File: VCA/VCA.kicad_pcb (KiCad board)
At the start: 2 copper layers, 40 x 200 mm, 57 parts, among them J1 EuroPower, J2 CV1, J3 IN1, J4 OUT1, J5 CV2, J6 IN2, J7 OUT2, U1 LM13700, U2 TL082, U3 TL082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

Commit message: updated footprints on VCA
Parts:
- J2, J3, J4, J5, J6, J7: footprint telec:JackHole -> telec:Jack_Hole_Square
- RV1, RV2, RV4, RV5: footprint Potentiometer_THT:Potentiometer_Piher_T-16L_Single_Vertical_Hole -> telec:Potentiometer_Single_Vertical_Hole
- moved RV4 13.3 mm to (41.7, 139.7), turned to 0 degrees
- moved RV5 13.1 mm to (22.1, 139.7), turned to 0 degrees
- moved RV1 12.9 mm to (42.0, 41.4), turned to 0 degrees
- moved RV2 12.8 mm to (22.6, 41.3), turned to 0 degrees
- moved R18 3.41 mm to (32.4, 136.6), turned to 90 degrees
- moved C2 1.50 mm to (39.5, 130.5)
- moved R8 0.31 mm to (43.2, 57.4)
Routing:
- net +12V: track 244.5 -> 250.5 mm
- net /IN1: track 32.2 -> 27.6 mm
- net /IN2: track 32.2 -> 27.6 mm
- net -12V: track 175.6 -> 177.9 mm
- net /CV2: track 25.5 -> 27.3 mm
- net GND: track 3.61 -> 2.37 mm
- net Net-(R18-Pad2): track 2.52 -> 3.63 mm
- net Net-(R19-Pad2): track 25.1 -> 26.2 mm
- net Net-(R12-Pad1): track 16.6 -> 15.7 mm
- net Net-(J4-PadT): track 4.30 -> 5.16 mm
- net Net-(R1-Pad1): track 15.7 -> 15.1 mm
- net /CV1: track 25.6 -> 26.1 mm
- net (no net): vias 0 -> 1

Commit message: VCA ready for prod
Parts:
- R10: value 150k -> 120k
- R11: value 27k -> 220k
- R7: value 10k -> 12k
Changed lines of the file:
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@@
   )
   (setup
-    (last_trace_width 1.016)
+    (last_trace_width 0.1524)
     (user_trace_width 0.1524)
     (user_trace_width 0.254)
@@
       (effects (font (size 1 1) (thickness 0.15)) (justify mirror))
     )
-    (fp_text value 10k (at 0 1.82) (layer B.SilkS)
+    (fp_text value 12k (at 0 1.82) (layer B.SilkS)
       (effects (font (size 1 1) (thickness 0.15)) (justify mirror))
     )
@@
       (effects (font (size 1 1) (thickness 0.15)) (justify mirror))
     )
-    (fp_text value 27k (at 0.1125 1.4) (layer B.SilkS)
+    (fp_text value 220k (at 0.1125 1.4) (layer B.SilkS)
       (effects (font (size 1 1) (thickness 0.15)) (justify mirror))
     )
@@
       (effects (font (size 1 1) (thickness 0.15)) (justify mirror))
     )
-    (fp_text value 150k (at 1.4875 1.6) (layer B.SilkS)
+    (fp_text value 120k (at 1.4875 1.6) (layer B.SilkS)
       (effects (font (size 1 1) (thickness 0.15)) (justify mirror))
     )
@@
     (arrow2b (pts (xy 12 6) (xy 13.126504 5.413579)))
   )
+  (via (at 46.6 60.4) (size 0.8) (drill 0.4) (layers F.Cu B.Cu) (net 0))
   (via (at 14.5 107.5) (size 0.8) (drill 0.4) (layers F.Cu B.Cu) (net 1))
   (via (at 33.2 107.7) (size 0.8) (drill 0.4) (layers F.Cu B.Cu) (net 1))
@@
   (segment (start 29.3 103.7) (end 32.4 100.6) (width 0.508) (layer F.Cu) (net 1))
   (segment (start 32.4 100.6) (end 32.4 97.5) (width 0.508) (layer F.Cu) (net 1))
+  (segment (start 48.169999 52.230001) (end 47 53.4) (width 1.016) (layer F.Cu) (net 1))
+  (segment (start 27.9 27.3) (end 27.9 24.304) (width 1.016) (layer F.Cu) (net 1))
+  (segment (start 28.968001 23.235999) (end 38.791521 23.235999) (width 1.016) (layer F.Cu) (net 1))
+  (segment (start 27.9 24.304) (end 28.968001 23.235999) (width 1.016) (layer F.Cu) (net 1))
+  (segment (start 38.791521 23.235999) (end 48.169999 32.614477) (width 1.016) (layer F.Cu) (net 1))
+  (segment (start 38.125 62.925) (end 39.395 62.925) (width 1.016) (layer F.Cu) (net 1))
+  (segment (start 39.5 55.2) (end 36.5 58.2) (width 1.016) (layer F.Cu) (net 1))
+  (segment (start 48.169999 32.614477) (end 48.169999 44.130001) (width 1.016) (layer F.Cu) (net 1))
+  (segment (start 36.5 58.2) (end 36.5 61.3) (width 1.016) (layer F.Cu) (net 1))
+  (segment (start 48.169999 44.130001) (end 48.169999 46.630001) (width 1.016) (layer F.Cu) (net 1))
+  (segment (start 36.5 61.3) (end 38.125 62.925) (width 1.016) (layer F.Cu) (net 1))
+  (segment (start 39.5 52.4) (end 39.5 55.2) (width 1.016) (layer F.Cu) (net 1))
+  (segment (start 48.169999 44.130001) (end 48.169999 52.230001) (width 1.016) (layer F.Cu) (net 1))
+  (segment (start 41.2 50.7) (end 39.5 52.4) (width 1.016) (layer F.Cu) (net 1))
+  (segment (start 48.169999 46.630001) (end 44.1 50.7) (width 1.016) (layer F.Cu) (net 1))
+  (segment (start 44.1 50.7) (end 41.2 50.7) (width 1.016) (layer F.Cu) (net 1))
+  (segment (start 44.299291 149.299291) (end 46.7 151.7) (width 1.016) (layer F.Cu) (net 1))
+  (segment (start 37.300709 149.299291) (end 44.299291 149.299291) (width 1.016) (layer F.Cu) (net 1))
+  (segment (start 37.300709 149.299291) (end 37.9 149.9) (width 1.016) (layer F.Cu) (net 1))
+  (segment (start 34.1 146.091006) (end 37.300709 149.299291) (width 1.016) (layer F.Cu) (net 1))
+  (via (at 32.4 138.0875) (size 0.8) (drill 0.4) (layers F.Cu B.Cu) (net 1))
+  (segment (start 36.575 128.45) (end 36.575 133.9125) (width 1.016) (layer B.Cu) (net 1))
+  (segment (start 36.575 133.9125) (end 32.4 138.0875) (width 1.016) (layer B.Cu) (net 1))
+  (segment (start 32.4 144.391006) (end 34.1 146.091006) (width 1.016) (layer F.Cu) (net 1))
+  (segment (start 32.4 138.0875) (end 32.4 144.391006) (width 1.016) (layer F.Cu) (net 1))
   (via (at 40 132.6) (size 0.8) (drill 0.4) (layers F.Cu B.Cu) (net 2))
   (via (at 40 126.5) (size 0.8) (drill 0.4) (layers F.Cu B.Cu) (net 2))
@@
   (via (at 50.6 69.2) (size 0.8) (drill 0.4) (layers F.Cu B.Cu) (net 2))
   (via (at 50.9 60.1) (size 0.8) (drill 0.4) (layers F.Cu B.Cu) (net 2))
-  (via (at 46.6 60.4) (size 0.8) (drill 0.4) (layers F.Cu B.Cu) (net 0))
-  (segment (start 48.169999 52.230001) (end 47 53.4) (width 1.016) (layer F.Cu) (net 1))
-  (segment (start 27.9 27.3) (end 27.9 24.304) (width 1.016) (layer F.Cu) (net 1))
-  (segment (start 28.968001 23.235999) (end 38.791521 23.235999) (width 1.016) (layer F.Cu) (net 1))
-  (segment (start 27.9 24.304) (end 28.968001 23.235999) (width 1.016) (layer F.Cu) (net 1))
-  (segment (start 38.791521 23.235999) (end 48.169999 32.614477) (width 1.016) (layer F.Cu) (net 1))
-  (segment (start 38.125 62.925) (end 39.395 62.925) (width 1.016) (layer F.Cu) (net 1))
-  (segment (start 39.5 55.2) (end 36.5 58.2) (width 1.016) (layer F.Cu) (net 1))
-  (segment (start 48.169999 32.614477) (end 48.169999 44.130001) (width 1.016) (layer F.Cu) (net 1))
-  (segment (start 36.5 58.2) (end 36.5 61.3) (width 1.016) (layer F.Cu) (net 1))
-  (segment (start 48.169999 44.130001) (end 48.169999 46.630001) (width 1.016) (layer F.Cu) (net 1))
-  (segment (start 36.5 61.3) (end 38.125 62.925) (width 1.016) (layer F.Cu) (net 1))
-  (segment (start 39.5 52.4) (end 39.5 55.2) (width 1.016) (layer F.Cu) (net 1))
-  (segment (start 48.169999 44.130001) (end 48.169999 52.230001) (width 1.016) (layer F.Cu) (net 1))
-  (segment (start 41.2 50.7) (end 39.5 52.4) (width 1.016) (layer F.Cu) (net 1))
-  (segment (start 48.169999 46.630001) (end 44.1 50.7) (width 1.016) (layer F.Cu) (net 1))
-  (segment (start 44.1 50.7) (end 41.2 50.7) (width 1.016) (layer F.Cu) (net 1))
-  (segment (start 44.299291 149.299291) (end 46.7 151.7) (width 1.016) (layer F.Cu) (net 1))
-  (segment (start 37.300709 149.299291) (end 44.299291 149.299291) (width 1.016) (layer F.Cu) (net 1))
-  (segment (start 37.300709 149.299291) (end 37.9 149.9) (width 1.016) (layer F.Cu) (net 1))
-  (segment (start 34.1 146.091006) (end 37.300709 149.299291) (width 1.016) (layer F.Cu) (net 1))
-  (via (at 32.4 138.0875) (size 0.8) (drill 0.4) (layers F.Cu B.Cu) (net 1))
-  (segment (start 36.575 128.45) (end 36.575 133.9125) (width 1.016) (layer B.Cu) (net 1))
-  (segment (start 36.575 133.9125) (end 32.4 138.0875) (width 1.016) (layer B.Cu) (net 1))
-  (segment (start 32.4 144.391006) (end 34.1 146.091006) (width 1.016) (layer F.Cu) (net 1))
-  (segment (start 32.4 138.0875) (end 32.4 144.391006) (width 1.016) (layer F.Cu) (net 1))
   (via (at 48.6 89.2) (size 0.8) (drill 0.4) (layers F.Cu B.Cu) (net 2))
   (via (at 48.6 97.7) (size 0.8) (drill 0.4) (layers F.Cu B.Cu) (net 2))

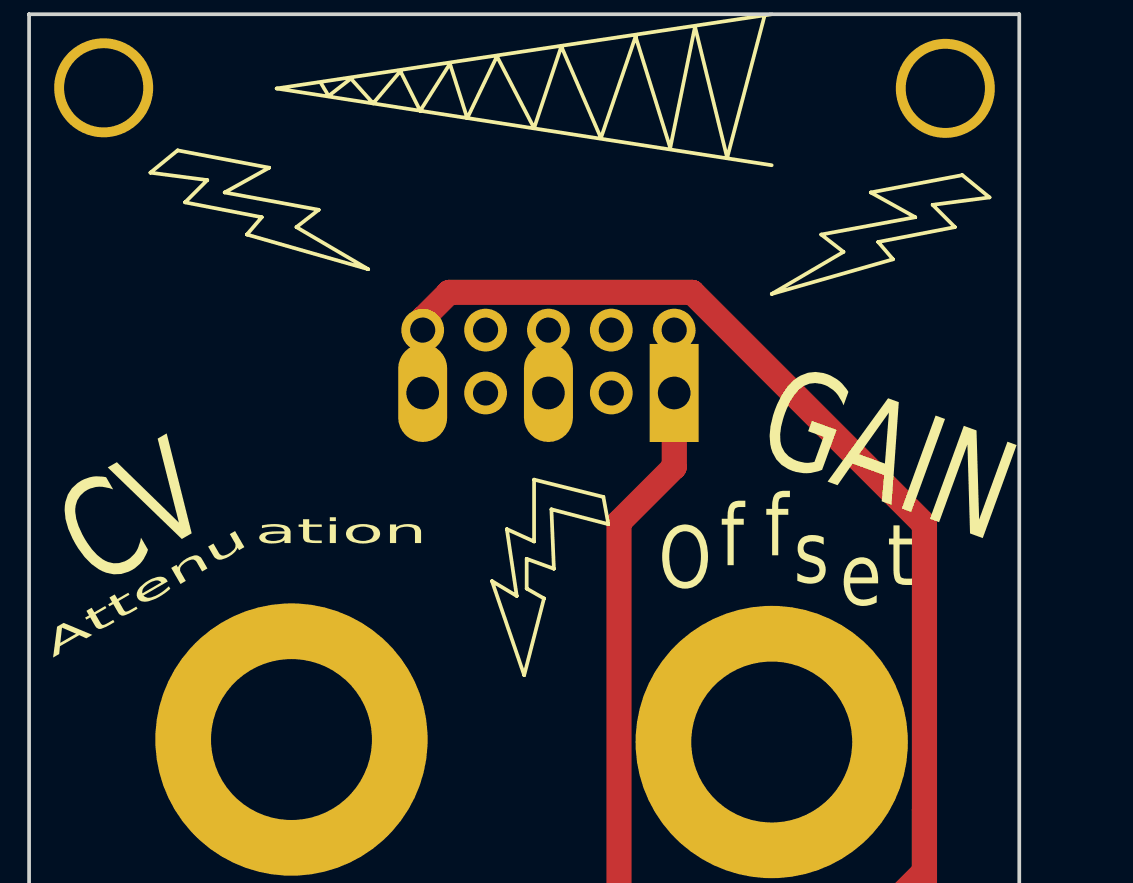
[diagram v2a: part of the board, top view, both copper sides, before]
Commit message: More clearance
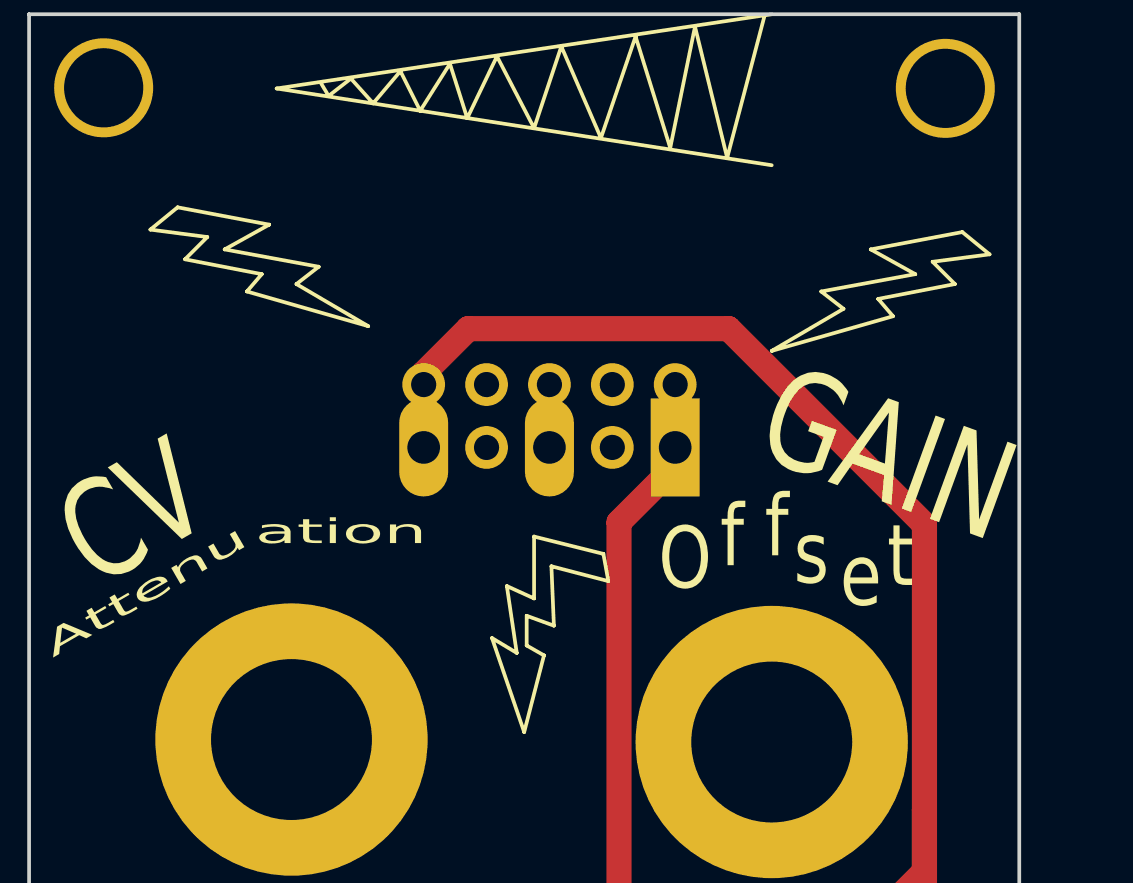
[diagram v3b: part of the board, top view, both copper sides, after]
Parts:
- moved J1 2.20 mm to (38.1, 29.5)
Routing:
- net -12V: track 177.9 -> 175.4 mm
- net +12V: track 250.5 -> 252.7 mm
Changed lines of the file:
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@@
   (general
     (thickness 1.6)
-    (drawings 154)
+    (drawings 157)
     (tracks 356)
     (zones 0)
@@
   )
   (setup
-    (last_trace_width 0.1524)
+    (last_trace_width 1.016)
     (user_trace_width 0.1524)
     (user_trace_width 0.254)
@@
   )
   (module telec:EuroPower (layer B.Cu)
-    (at 38.06 27.3 90)
+    (at 38.1 29.5 90)
     (fp_text reference J1 (at 1.397 6.35 270) (layer B.SilkS)
       (effects (font (size 1 1) (thickness 0.15)) (justify mirror))
@@
       (rotate (xyz 0 0 0))
     )
+  )
+  (gr_line (start 52 23) (end 11.9 23) (layer F.Fab) (width 0.15))
+  (dimension 11 (width 0.15) (layer F.Fab)
+    (gr_text "11,000 mm" (at 55.7 17.5 270) (layer F.Fab)
+      (effects (font (size 1 1) (thickness 0.15)))
+    )
+    (feature1 (pts (xy 52 23) (xy 54.986421 23)))
+    (feature2 (pts (xy 52 12) (xy 54.986421 12)))
+    (crossbar (pts (xy 54.4 12) (xy 54.4 23)))
+    (arrow1a (pts (xy 54.4 23) (xy 53.813579 21.873496)))
+    (arrow1b (pts (xy 54.4 23) (xy 54.986421 21.873496)))
+    (arrow2a (pts (xy 54.4 12) (xy 53.813579 13.126504)))
+    (arrow2b (pts (xy 54.4 12) (xy 54.986421 13.126504)))
+  )
+  (dimension 12.7 (width 0.15) (layer F.Fab)
+    (gr_text "12,700 mm" (at 55.1 205.65 90) (layer F.Fab)
+      (effects (font (size 1 1) (thickness 0.15)))
+    )
+    (feature1 (pts (xy 52 199.3) (xy 54.386421 199.3)))
+    (feature2 (pts (xy 52 212) (xy 54.386421 212)))
+    (crossbar (pts (xy 53.8 212) (xy 53.8 199.3)))
+    (arrow1a (pts (xy 53.8 199.3) (xy 54.386421 200.426504)))
+    (arrow1b (pts (xy 53.8 199.3) (xy 53.213579 200.426504)))
+    (arrow2a (pts (xy 53.8 212) (xy 54.386421 210.873496)))
+    (arrow2b (pts (xy 53.8 212) (xy 53.213579 210.873496)))
   )
   (gr_line (start 12.3 202.8) (end 32.1 202.8) (layer F.SilkS) (width 0.5))
@@
     (effects (font (size 4 3) (thickness 0.4)))
   )
-  (gr_line (start 46 19.2) (end 47.8 20.2) (layer F.SilkS) (width 0.15))
-  (gr_line (start 47.8 20.2) (end 44 20.9) (layer F.SilkS) (width 0.15))
-  (gr_line (start 46.3 21.2) (end 49.4 20.6) (layer F.SilkS) (width 0.15))
-  (gr_line (start 44.9 21.6) (end 42 23.3) (layer F.SilkS) (width 0.15))
-  (gr_line (start 44 20.9) (end 44.9 21.6) (layer F.SilkS) (width 0.15))
-  (gr_line (start 49.4 20.6) (end 48.5 19.7) (layer F.SilkS) (width 0.15))
-  (gr_line (start 48.5 19.7) (end 50.8 19.4) (layer F.SilkS) (width 0.15))
-  (gr_line (start 46.9 21.9) (end 46.3 21.2) (layer F.SilkS) (width 0.15))
-  (gr_line (start 50.8 19.4) (end 49.7 18.5) (layer F.SilkS) (width 0.15))
-  (gr_line (start 42 23.3) (end 46.9 21.9) (layer F.SilkS) (width 0.15))
-  (gr_line (start 49.7 18.5) (end 46 19.2) (layer F.SilkS) (width 0.15))
-  (gr_line (start 35.4 32.6) (end 35.2 31.5) (layer F.SilkS) (width 0.15))
-  (gr_line (start 33.1 32) (end 35.4 32.6) (layer F.SilkS) (width 0.15))
-  (gr_line (start 33.2 34.4) (end 33.1 32) (layer F.SilkS) (width 0.15))
-  (gr_line (start 32.1 34) (end 33.2 34.4) (layer F.SilkS) (width 0.15))
-  (gr_line (start 32.1 35.2) (end 32.1 34) (layer F.SilkS) (width 0.15))
-  (gr_line (start 32.8 35.6) (end 32.1 35.2) (layer F.SilkS) (width 0.15))
-  (gr_line (start 32 38.7) (end 32.8 35.6) (layer F.SilkS) (width 0.15))
-  (gr_line (start 30.7 34.9) (end 32 38.7) (layer F.SilkS) (width 0.15))
-  (gr_line (start 31.7 35.5) (end 30.7 34.9) (layer F.SilkS) (width 0.15))
-  (gr_line (start 31.3 32.8) (end 31.7 35.5) (layer F.SilkS) (width 0.15))
-  (gr_line (start 32.4 33.3) (end 31.3 32.8) (layer F.SilkS) (width 0.15))
-  (gr_line (start 32.4 30.8) (end 32.4 33.3) (layer F.SilkS) (width 0.15))
-  (gr_line (start 35.2 31.5) (end 32.4 30.8) (layer F.SilkS) (width 0.15))
-  (gr_line (start 19.2 18.7) (end 16.9 18.4) (layer F.SilkS) (width 0.15))
-  (gr_line (start 18.3 19.6) (end 19.2 18.7) (layer F.SilkS) (width 0.15))
-  (gr_line (start 21.4 20.2) (end 18.3 19.6) (layer F.SilkS) (width 0.15))
-  (gr_line (start 20.8 20.9) (end 21.4 20.2) (layer F.SilkS) (width 0.15))
-  (gr_line (start 25.7 22.3) (end 20.8 20.9) (layer F.SilkS) (width 0.15))
-  (gr_line (start 22.8 20.6) (end 25.7 22.3) (layer F.SilkS) (width 0.15))
-  (gr_line (start 23.7 19.9) (end 22.8 20.6) (layer F.SilkS) (width 0.15))
-  (gr_line (start 19.9 19.2) (end 23.7 19.9) (layer F.SilkS) (width 0.15))
-  (gr_line (start 21.7 18.2) (end 19.9 19.2) (layer F.SilkS) (width 0.15))
-  (gr_line (start 18 17.5) (end 21.7 18.2) (layer F.SilkS) (width 0.15))
-  (gr_line (start 16.9 18.4) (end 18 17.5) (layer F.SilkS) (width 0.15))
+  (gr_line (start 46 21.5) (end 47.8 22.5) (layer F.SilkS) (width 0.15))
+  (gr_line (start 47.8 22.5) (end 44 23.2) (layer F.SilkS) (width 0.15))
+  (gr_line (start 46.3 23.5) (end 49.4 22.9) (layer F.SilkS) (width 0.15))
+  (gr_line (start 44.9 23.9) (end 42 25.6) (layer F.SilkS) (width 0.15))
+  (gr_line (start 44 23.2) (end 44.9 23.9) (layer F.SilkS) (width 0.15))
+  (gr_line (start 49.4 22.9) (end 48.5 22) (layer F.SilkS) (width 0.15))
+  (gr_line (start 48.5 22) (end 50.8 21.7) (layer F.SilkS) (width 0.15))
+  (gr_line (start 46.9 24.2) (end 46.3 23.5) (layer F.SilkS) (width 0.15))
+  (gr_line (start 50.8 21.7) (end 49.7 20.8) (layer F.SilkS) (width 0.15))
+  (gr_line (start 42 25.6) (end 46.9 24.2) (layer F.SilkS) (width 0.15))
+  (gr_line (start 49.7 20.8) (end 46 21.5) (layer F.SilkS) (width 0.15))
+  (gr_line (start 35.4 34.9) (end 35.2 33.8) (layer F.SilkS) (width 0.15))
+  (gr_line (start 33.1 34.3) (end 35.4 34.9) (layer F.SilkS) (width 0.15))
+  (gr_line (start 33.2 36.7) (end 33.1 34.3) (layer F.SilkS) (width 0.15))
+  (gr_line (start 32.1 36.3) (end 33.2 36.7) (layer F.SilkS) (width 0.15))
+  (gr_line (start 32.1 37.5) (end 32.1 36.3) (layer F.SilkS) (width 0.15))
+  (gr_line (start 32.8 37.9) (end 32.1 37.5) (layer F.SilkS) (width 0.15))
+  (gr_line (start 32 41) (end 32.8 37.9) (layer F.SilkS) (width 0.15))
+  (gr_line (start 30.7 37.2) (end 32 41) (layer F.SilkS) (width 0.15))
+  (gr_line (start 31.7 37.8) (end 30.7 37.2) (layer F.SilkS) (width 0.15))
+  (gr_line (start 31.3 35.1) (end 31.7 37.8) (layer F.SilkS) (width 0.15))
+  (gr_line (start 32.4 35.6) (end 31.3 35.1) (layer F.SilkS) (width 0.15))
+  (gr_line (start 32.4 33.1) (end 32.4 35.6) (layer F.SilkS) (width 0.15))
+  (gr_line (start 35.2 33.8) (end 32.4 33.1) (layer F.SilkS) (width 0.15))
+  (gr_line (start 19.2 21) (end 16.9 20.7) (layer F.SilkS) (width 0.15))
+  (gr_line (start 18.3 21.9) (end 19.2 21) (layer F.SilkS) (width 0.15))
+  (gr_line (start 21.4 22.5) (end 18.3 21.9) (layer F.SilkS) (width 0.15))
+  (gr_line (start 20.8 23.2) (end 21.4 22.5) (layer F.SilkS) (width 0.15))
+  (gr_line (start 25.7 24.6) (end 20.8 23.2) (layer F.SilkS) (width 0.15))
+  (gr_line (start 22.8 22.9) (end 25.7 24.6) (layer F.SilkS) (width 0.15))
+  (gr_line (start 23.7 22.2) (end 22.8 22.9) (layer F.SilkS) (width 0.15))
+  (gr_line (start 19.9 21.5) (end 23.7 22.2) (layer F.SilkS) (width 0.15))
+  (gr_line (start 21.7 20.5) (end 19.9 21.5) (layer F.SilkS) (width 0.15))
+  (gr_line (start 18 19.8) (end 21.7 20.5) (layer F.SilkS) (width 0.15))
+  (gr_line (start 16.9 20.7) (end 18 19.8) (layer F.SilkS) (width 0.15))
   (gr_text "Offset 2" (at 45.9 125.6) (layer B.SilkS)
     (effects (font (size 1 1) (thickness 0.15)) (justify mirror))
@@
   (gr_line (start 30.7 132.8) (end 24.6 132.8) (layer B.SilkS) (width 0.15))
   (gr_line (start 30.7 126.4) (end 30.7 132.8) (layer B.SilkS) (width 0.15))
-  (gr_text +12V (at 33.2 15.2 45) (layer B.SilkS)
+  (gr_text +12V (at 33 17.4 45) (layer B.SilkS)
     (effects (font (size 2 2) (thickness 0.5)) (justify left mirror))
   )
-  (gr_text -12V (at 43.6 15.2 45) (layer B.SilkS)
+  (gr_text -12V (at 43.4 17.4 45) (layer B.SilkS)
     (effects (font (size 2 2) (thickness 0.5)) (justify left mirror))
   )
-  (gr_text GND (at 38.8 15 45) (layer B.SilkS)
+  (gr_text GND (at 38.6 17.2 45) (layer B.SilkS)
     (effects (font (size 2 2.8) (thickness 0.5)) (justify left mirror))
   )
@@
   (segment (start 32.4 100.6) (end 32.4 97.5) (width 0.508) (layer F.Cu) (net 1))
   (segment (start 48.169999 52.230001) (end 47 53.4) (width 1.016) (layer F.Cu) (net 1))
-  (segment (start 27.9 27.3) (end 27.9 24.304) (width 1.016) (layer F.Cu) (net 1))
-  (segment (start 28.968001 23.235999) (end 38.791521 23.235999) (width 1.016) (layer F.Cu) (net 1))
-  (segment (start 27.9 24.304) (end 28.968001 23.235999) (width 1.016) (layer F.Cu) (net 1))
-  (segment (start 38.791521 23.235999) (end 48.169999 32.614477) (width 1.016) (layer F.Cu) (net 1))
   (segment (start 38.125 62.925) (end 39.395 62.925) (width 1.016) (layer F.Cu) (net 1))
   (segment (start 39.5 55.2) (end 36.5 58.2) (width 1.016) (layer F.Cu) (net 1))
@@
   (segment (start 32.4 144.391006) (end 34.1 146.091006) (width 1.016) (layer F.Cu) (net 1))
   (segment (start 32.4 138.0875) (end 32.4 144.391006) (width 1.016) (layer F.Cu) (net 1))
+  (segment (start 27.94 26.96) (end 27.94 29.5) (width 1.016) (layer F.Cu) (net 1))
+  (segment (start 48.169999 32.614477) (end 40.255522 24.7) (width 1.016) (layer F.Cu) (net 1))
+  (segment (start 27.94 26.504) (end 27.94 29.5) (width 1.016) (layer F.Cu) (net 1))
+  (segment (start 40.255522 24.7) (end 29.744 24.7) (width 1.016) (layer F.Cu) (net 1))
+  (segment (start 29.744 24.7) (end 27.94 26.504) (width 1.016) (layer F.Cu) (net 1))
   (via (at 40 132.6) (size 0.8) (drill 0.4) (layers F.Cu B.Cu) (net 2))
   (via (at 40 126.5) (size 0.8) (drill 0.4) (layers F.Cu B.Cu) (net 2))
@@
   (segment (start 43.255 157.955) (end 43.255 166.625) (width 1.016) (layer B.Cu) (net 3))
   (segment (start 37.1 151.8) (end 43.255 157.955) (width 1.016) (layer B.Cu) (net 3))
-  (segment (start 38.06 24.76) (end 38.06 27.3) (width 1.016) (layer F.Cu) (net 3))
   (segment (start 37 53.3) (end 43.205 59.505) (width 1.016) (layer B.Cu) (net 3))
   (segment (start 43.205 59.505) (end 43.205 67.875) (width 1.016) (layer B.Cu) (net 3))
